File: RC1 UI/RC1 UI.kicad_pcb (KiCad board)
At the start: 2 copper layers, 99.1 x 99.1 mm, 56 parts, among them J1 KB, J2 RC1_UI_Port, J3 COM, M1 Mounting, M2 Mounting, M3 Mounting, M4 Mounting, Q1 2N3906, Q2 2N3906, Q3 2N3906, Q4 2N3906, Q5 2N3906, Q6 2N3906, U1 74LS145, U2 74LS06, U3 74LS38, U4 74LS00

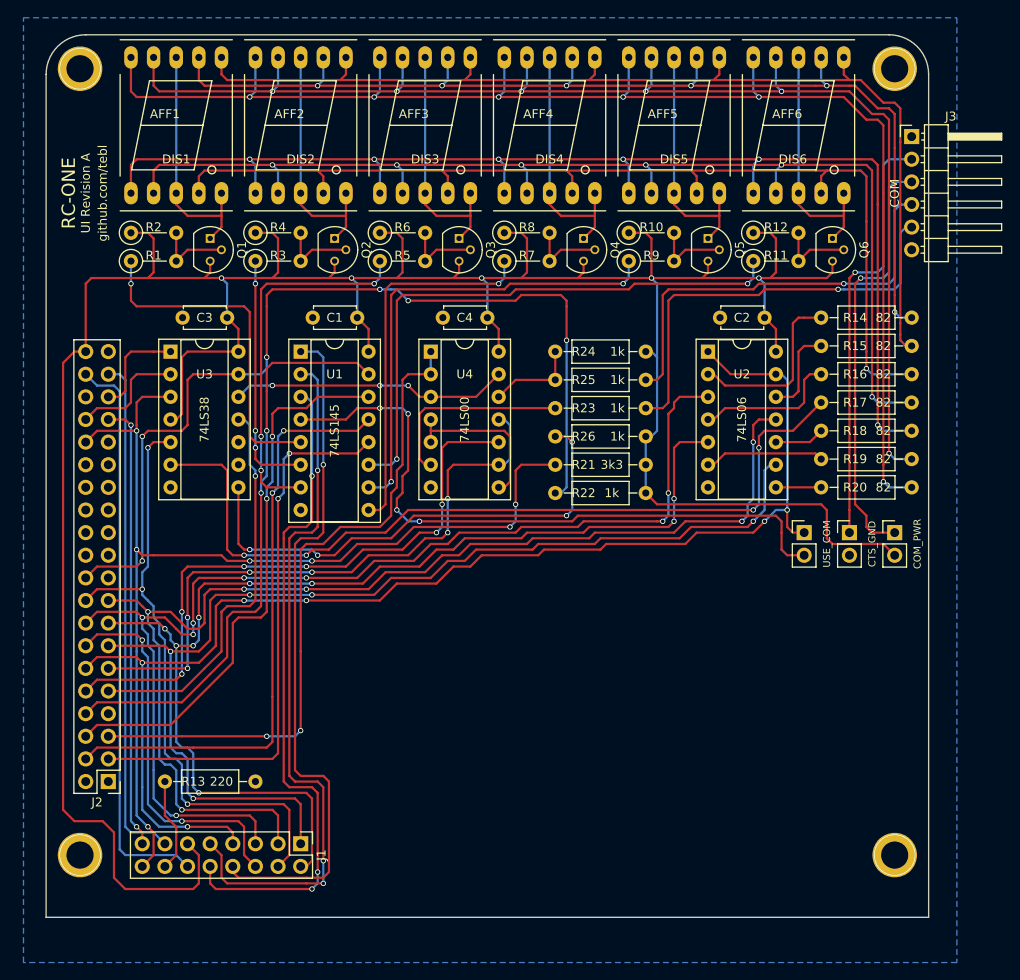
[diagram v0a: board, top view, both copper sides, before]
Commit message: Tweaked silkscreens and exported gerbers for CPU/UI
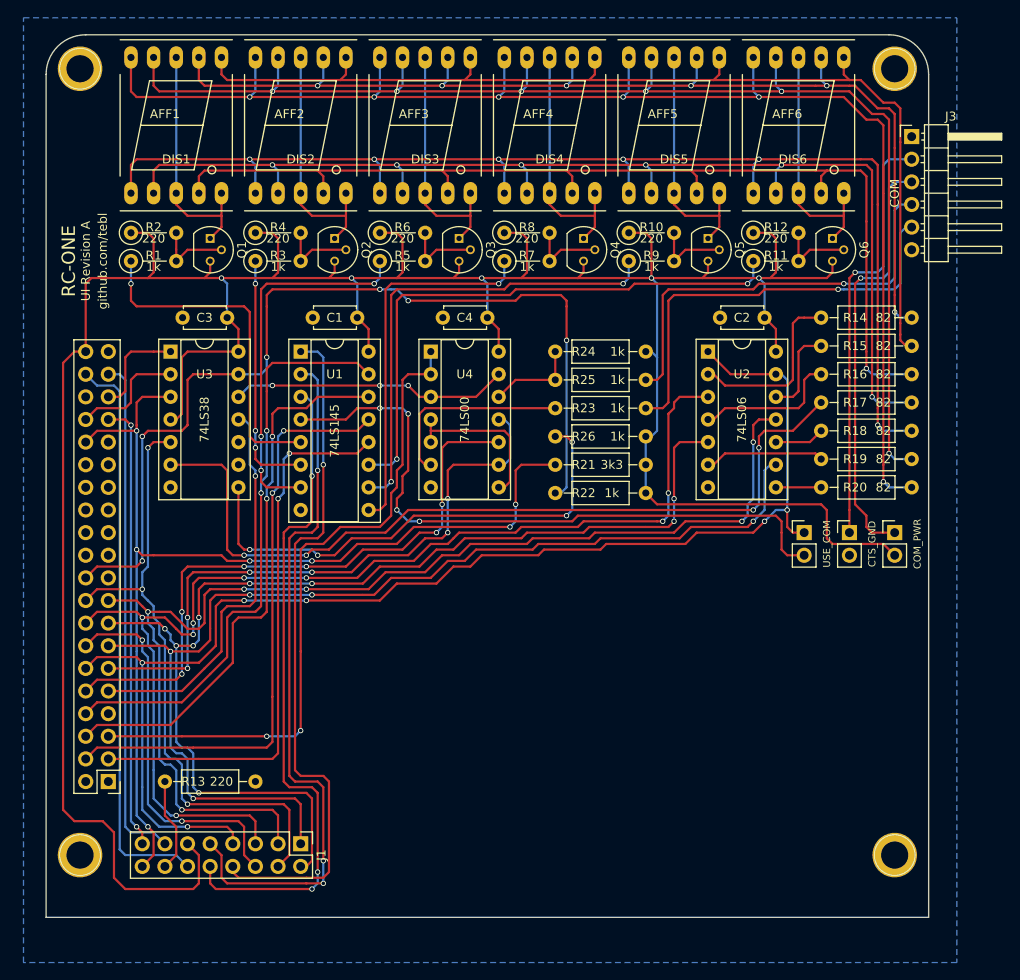
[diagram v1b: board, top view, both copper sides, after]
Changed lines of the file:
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@@
     (descr "Through hole straight pin header, 2x20, 2.54mm pitch, double rows")
     (tags "Through hole pin header THT 2x20 2.54mm double row")
-    (fp_text reference J2 (at 1.27 -2.33 180) (layer F.SilkS)
-      (effects (font (size 1 1) (thickness 0.15)))
-    )
-    (fp_text value RC1_UI_Port (at 1.27 50.59 180) (layer F.Fab)
+    (fp_text reference J2 (at 1.27 -2.54 180) (layer F.Fab)
+      (effects (font (size 1 1) (thickness 0.15)))
+    )
+    (fp_text value RC1_UI_Port (at 1.27 50.8 180) (layer F.Fab)
       (effects (font (size 1 1) (thickness 0.15)))
     )
@@
       (effects (font (size 1 1) (thickness 0.15)))
     )
-    (fp_text value 1k (at 2.54 0.635) (layer F.Fab)
+    (fp_text value 1k (at 2.54 0.635) (layer F.SilkS)
       (effects (font (size 1 1) (thickness 0.15)))
     )
@@
       (effects (font (size 1 1) (thickness 0.15)))
     )
-    (fp_text value 220 (at 2.54 0.635) (layer F.Fab)
+    (fp_text value 220 (at 2.54 0.635) (layer F.SilkS)
       (effects (font (size 1 1) (thickness 0.15)))
     )
@@
       (effects (font (size 1 1) (thickness 0.15)))
     )
-    (fp_text value 1k (at 2.54 0.635) (layer F.Fab)
+    (fp_text value 1k (at 2.54 0.635) (layer F.SilkS)
       (effects (font (size 1 1) (thickness 0.15)))
     )
@@
       (effects (font (size 1 1) (thickness 0.15)))
     )
-    (fp_text value 220 (at 2.54 0.635) (layer F.Fab)
+    (fp_text value 220 (at 2.54 0.635) (layer F.SilkS)
       (effects (font (size 1 1) (thickness 0.15)))
     )
@@
       (effects (font (size 1 1) (thickness 0.15)))
     )
-    (fp_text value 1k (at 2.54 0.635) (layer F.Fab)
+    (fp_text value 1k (at 2.54 0.635) (layer F.SilkS)
       (effects (font (size 1 1) (thickness 0.15)))
     )
@@
       (effects (font (size 1 1) (thickness 0.15)))
     )
-    (fp_text value 220 (at 2.54 0.635) (layer F.Fab)
+    (fp_text value 220 (at 2.54 0.635) (layer F.SilkS)
       (effects (font (size 1 1) (thickness 0.15)))
     )
@@
       (effects (font (size 1 1) (thickness 0.15)))
     )
-    (fp_text value 1k (at 2.54 0.635) (layer F.Fab)
+    (fp_text value 1k (at 2.54 0.635) (layer F.SilkS)
       (effects (font (size 1 1) (thickness 0.15)))
     )
@@
       (effects (font (size 1 1) (thickness 0.15)))
     )
-    (fp_text value 220 (at 2.54 0.635) (layer F.Fab)
+    (fp_text value 220 (at 2.54 0.635) (layer F.SilkS)
       (effects (font (size 1 1) (thickness 0.15)))
     )
@@
       (effects (font (size 1 1) (thickness 0.15)))
     )
-    (fp_text value 1k (at 2.54 0.635) (layer F.Fab)
+    (fp_text value 1k (at 2.54 0.635) (layer F.SilkS)
       (effects (font (size 1 1) (thickness 0.15)))
     )
@@
       (effects (font (size 1 1) (thickness 0.15)))
     )
-    (fp_text value 220 (at 2.54 0.635) (layer F.Fab)
+    (fp_text value 220 (at 2.54 0.635) (layer F.SilkS)
       (effects (font (size 1 1) (thickness 0.15)))
     )
@@
       (effects (font (size 1 1) (thickness 0.15)))
     )
-    (fp_text value 1k (at 2.54 0.635) (layer F.Fab)
+    (fp_text value 1k (at 2.54 0.635) (layer F.SilkS)
       (effects (font (size 1 1) (thickness 0.15)))
     )
@@
       (effects (font (size 1 1) (thickness 0.15)))
     )
-    (fp_text value 220 (at 2.54 0.635) (layer F.Fab)
+    (fp_text value 220 (at 2.54 0.635) (layer F.SilkS)
       (effects (font (size 1 1) (thickness 0.15)))
     )
@@
     )
   )
-  (gr_text "UI Revision A" (at 112.395 54.61 90) (layer F.SilkS)
+  (gr_text "UI Revision A" (at 112.395 62.23 90) (layer F.SilkS)
     (effects (font (size 1 1) (thickness 0.15)))
   )
-  (gr_text github.com/tebl (at 114.3 54.61 90) (layer F.SilkS)
+  (gr_text github.com/tebl (at 114.3 62.23 90) (layer F.SilkS)
     (effects (font (size 1 1) (thickness 0.15)))
   )
-  (gr_text RC-ONE (at 110.49 54.61 90) (layer F.SilkS)
+  (gr_text RC-ONE (at 110.49 62.23 90) (layer F.SilkS)
     (effects (font (size 1.5 1.5) (thickness 0.3)))
   )

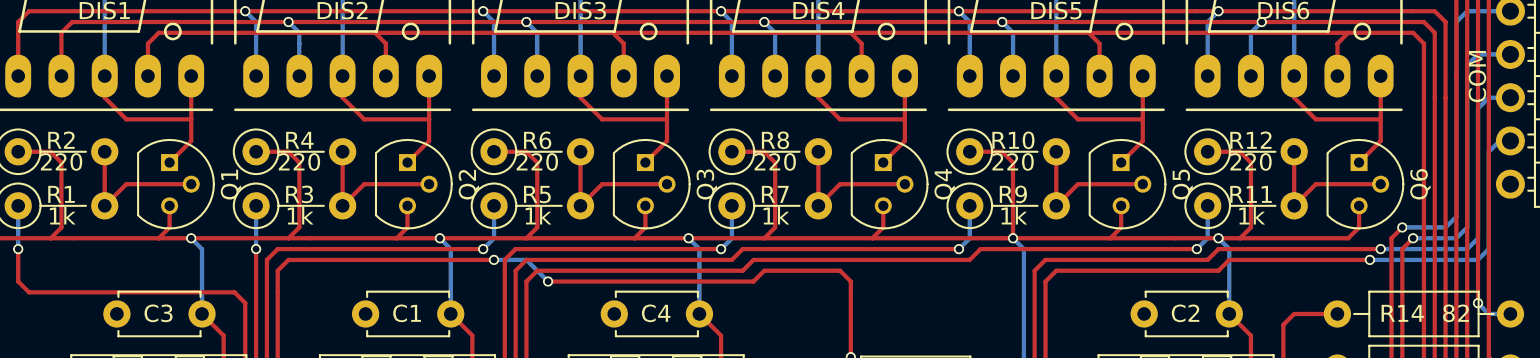
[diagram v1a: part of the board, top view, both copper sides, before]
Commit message: Moved transistors the right way around
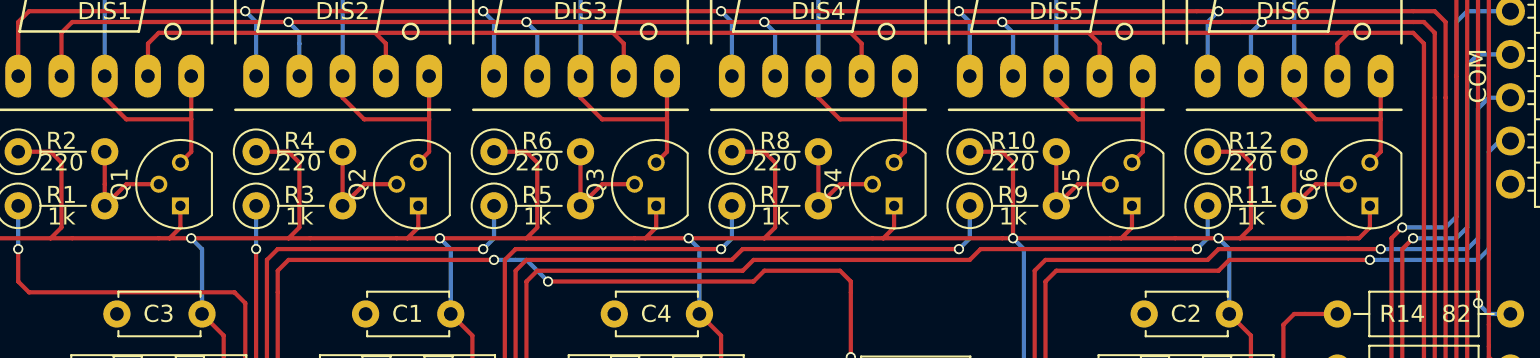
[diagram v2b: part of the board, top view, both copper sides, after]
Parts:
- moved Q1 2.62 mm to (127.0, 62.2), turned to 90 degrees
- moved Q2 2.62 mm to (141.0, 62.2), turned to 90 degrees
- moved Q3 2.62 mm to (154.9, 62.2), turned to 90 degrees
- moved Q4 2.62 mm to (168.9, 62.2), turned to 90 degrees
- moved Q5 2.62 mm to (182.9, 62.2), turned to 90 degrees
- moved Q6 2.62 mm to (196.8, 62.2), turned to 90 degrees
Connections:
- Q1 pad 1: Net-(AFF1-Pad3) -> VCC
- Q1 pad 3: VCC -> Net-(AFF1-Pad3)
- Q2 pad 1: Net-(AFF2-Pad3) -> VCC
- Q2 pad 3: VCC -> Net-(AFF2-Pad3)
- Q3 pad 1: Net-(AFF3-Pad3) -> VCC
- Q3 pad 3: VCC -> Net-(AFF3-Pad3)
- Q4 pad 1: Net-(AFF4-Pad3) -> VCC
- Q4 pad 3: VCC -> Net-(AFF4-Pad3)
- Q5 pad 1: Net-(AFF5-Pad3) -> VCC
- Q5 pad 3: VCC -> Net-(AFF5-Pad3)
- Q6 pad 1: Net-(AFF6-Pad3) -> VCC
- Q6 pad 3: VCC -> Net-(AFF6-Pad3)
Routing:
- net Net-(Q3-Pad2): track 8.78 -> 6.88 mm
- net Net-(Q2-Pad2): track 8.78 -> 6.88 mm
- net Net-(Q6-Pad2): track 8.78 -> 6.88 mm
- net Net-(Q4-Pad2): track 8.78 -> 6.88 mm
- net Net-(Q1-Pad2): track 8.78 -> 6.88 mm
- net Net-(Q5-Pad2): track 8.78 -> 6.88 mm
- net VCC: track 339.4 -> 340.1 mm
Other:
- board text added: "6x 2N3906"

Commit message: Layout updated
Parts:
- removed R10, R12: 220, Resistors_THT:R_Axial_DIN0207_L6.3mm_D2.5mm_P5.08mm_Vertical
- removed R11, R9: 1k, Resistors_THT:R_Axial_DIN0207_L6.3mm_D2.5mm_P5.08mm_Vertical
- removed R24: 1k, Resistors_THT:R_Axial_DIN0207_L6.3mm_D2.5mm_P10.16mm_Horizontal
- added C5: 100nF, Capacitors_THT:C_Disc_D4.7mm_W2.5mm_P5.00mm, F.Cu at (128.3, 68.6)
- added C6: 100nF, Capacitors_THT:C_Disc_D4.7mm_W2.5mm_P5.00mm, F.Cu at (189.2, 68.6)
- added J4: TAPE, Pin_Headers:Pin_Header_Straight_1x04_Pitch2.54mm, F.Cu at (156.2, 130.2)
- added JP4: DP_EN, Pin_Headers:Pin_Header_Straight_1x03_Pitch2.54mm, F.Cu at (200.0, 104.8)
- added JP5: SSD_EN, Pin_Headers:Pin_Header_Straight_1x03_Pitch2.54mm, F.Cu at (195.6, 104.8)
- added JP6: DP4_EN, Pin_Headers:Pin_Header_Straight_1x03_Pitch2.54mm, F.Cu at (204.5, 104.8)
- added U5: 74LS04, Housings_DIP:DIP-14_W7.62mm_Socket, F.Cu at (121.9, 72.4)
- added U6: 74LS244, Housings_DIP:DIP-20_W7.62mm_Socket, F.Cu at (182.9, 72.4)
- J1: value KB -> KEYPAD
- J3: moved to B.Cu
- JP2: value CTS_GND -> FlowControl; footprint Pin_Headers:Pin_Header_Straight_1x02_Pitch2.54mm -> Pin_Headers:Pin_Header_Angled_1x02_Pitch2.54mm; moved to B.Cu
- Q1, Q2, Q3, Q4, Q5, Q6: value 2N3906 -> 2N3904
- R1, R3, R5: value 1k -> 10k
- R14, R15, R16, R17, R18, R19, R20: value 82 -> 100
- R2, R4, R6: value 220 -> 10k
- R21: value 3k3 -> 10k
- R7: value 1k -> 100; footprint Resistors_THT:R_Axial_DIN0207_L6.3mm_D2.5mm_P5.08mm_Vertical -> Resistors_THT:R_Axial_DIN0207_L6.3mm_D2.5mm_P10.16mm_Horizontal
- R8: value 220 -> 100; footprint Resistors_THT:R_Axial_DIN0207_L6.3mm_D2.5mm_P5.08mm_Vertical -> Resistors_THT:R_Axial_DIN0207_L6.3mm_D2.5mm_P10.16mm_Horizontal
- U1: value 74LS145 -> 74LS138
- U2: value 74LS06 -> 74LS138; footprint Housings_DIP:DIP-14_W7.62mm_Socket -> Housings_DIP:DIP-16_W7.62mm_Socket
- U3: value 74LS38 -> 74LS01
- moved R8 54.5 mm to (194.9, 100.3)
- moved R22 47.6 mm to (134.6, 113.0), turned to 0 degrees
- moved R6 46.4 mm to (191.8, 59.1), turned to 180 degrees
- moved R26 46.4 mm to (144.8, 116.8)
- moved R21 38.9 mm to (134.6, 109.2)
- moved R7 37.8 mm to (194.9, 74.9)
- moved JP1 35.4 mm to (197.5, 127.6)
- moved C3 33.0 mm to (128.3, 101.6)
- moved U3 33.0 mm to (121.9, 105.4)
- moved R5 32.5 mm to (177.8, 59.1), turned to 180 degrees
- moved R4 32.4 mm to (163.8, 59.1), turned to 180 degrees
- moved C2 29.8 mm to (158.8, 68.6)
- moved U2 29.8 mm to (152.4, 72.4)
- moved JP2 28.8 mm to (205.1, 64.8)
- moved JP3 22.6 mm to (179.1, 74.9)
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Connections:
- AFF1 pad 5: Net-(AFF1-Pad3) -> /DP
- AFF2 pad 5: Net-(AFF2-Pad3) -> /DP
- AFF3 pad 5: Net-(AFF3-Pad3) -> /DP
- AFF4 pad 5: Net-(AFF4-Pad3) -> /DP4
- AFF5 pad 5: Net-(AFF5-Pad3) -> /DP
- AFF6 pad 5: Net-(AFF6-Pad3) -> /DP
- J1 pad 14: /KP_PWR -> Net-(J1-Pad14)
- J1 pad 15: SST_OUT -> SST_IN
- J1 pad 16: SST_IN -> SST_OUT
- J2 pad 20: TAPE -> (no net)
- J2 pad 32: SST_IN -> (no net)
- J2 pad 7: (no net) -> /PB6
- J3 pad 1: GND -> Net-(J3-Pad1)
- J3 pad 6: (no net) -> GND
- JP1 pad 1: Net-(J3-Pad3) -> Net-(J3-Pad4)
- JP2 pad 1: Net-(J3-Pad2) -> Net-(J3-Pad1)
- JP2 pad 2: GND -> Net-(J3-Pad5)
- JP3 pad 2: Net-(JP3-Pad2) -> /MODE
- Q1 pad 1: VCC -> GND
- Q2 pad 1: VCC -> GND
- Q3 pad 1: VCC -> GND
- Q4 pad 1: VCC -> GND
- Q5 pad 1: VCC -> GND
- Q6 pad 1: VCC -> GND
- R1 pad 1: Net-(R1-Pad1) -> Net-(Q1-Pad2)
- R1 pad 2: Net-(Q1-Pad2) -> /DIS1
- R13 pad 1: GND -> Net-(J1-Pad14)
- R13 pad 2: /KP_PWR -> GND
- R2 pad 1: VCC -> Net-(Q2-Pad2)
- R2 pad 2: Net-(Q1-Pad2) -> /DIS2
- R22 pad 1: VCC -> Net-(J4-Pad2)
- R22 pad 2: TAPE -> VCC
- R23 pad 1: Net-(J3-Pad5) -> /TX
- R23 pad 2: /TX -> Net-(J3-Pad2)
- R25 pad 1: Net-(J3-Pad4) -> /RX
- R25 pad 2: /RX -> Net-(J3-Pad3)
- R3 pad 1: Net-(R3-Pad1) -> Net-(Q3-Pad2)
- R3 pad 2: Net-(Q2-Pad2) -> /DIS3
- R4 pad 1: VCC -> Net-(Q4-Pad2)
- R4 pad 2: Net-(Q2-Pad2) -> /DIS4
- R5 pad 1: Net-(R5-Pad1) -> Net-(Q5-Pad2)
- R5 pad 2: Net-(Q3-Pad2) -> /DIS5
- R6 pad 1: VCC -> Net-(Q6-Pad2)
- R6 pad 2: Net-(Q3-Pad2) -> /DIS6
- R7 pad 2: Net-(Q4-Pad2) -> /DP
- R8 pad 2: Net-(Q4-Pad2) -> Net-(JP6-Pad1)
- U1 pad 1: /ROW0 -> /PB1
- U1 pad 12: /PB4 -> /MODE
- U1 pad 13: /PB3 -> /ROW2
- U1 pad 14: /PB2 -> /ROW1
- U1 pad 15: /PB1 -> /ROW0
- U1 pad 2: /ROW1 -> /PB2
- U1 pad 3: /ROW2 -> /PB3
- U1 pad 4: Net-(JP3-Pad2) -> GND
- U1 pad 5: Net-(R1-Pad1) -> /PB4
- U1 pad 6: Net-(R3-Pad1) -> VCC
- U1 pad 7: Net-(R5-Pad1) -> Net-(U1-Pad7)
- U1 pad 9: Net-(R7-Pad1) -> Net-(U1-Pad9)
- U2 pad 1: /PA0 -> /PB1
- U2 pad 10: Net-(R18-Pad1) -> (no net)
- U2 pad 11: /PA4 -> (no net)
- U2 pad 12: Net-(R15-Pad1) -> (no net)
- U2 pad 13: /PA0 -> (no net)
- U2 pad 14: VCC -> Net-(U2-Pad14)
- U2 pad 2: Net-(R14-Pad1) -> /PB2
- U2 pad 3: /PA2 -> /PB3
- U2 pad 4: Net-(R16-Pad1) -> GND
- U2 pad 5: /PA5 -> GND
- U2 pad 6: Net-(R19-Pad1) -> /PB4
- U2 pad 7: GND -> (no net)
- U2 pad 8: Net-(R20-Pad1) -> GND
- U2 pad 9: /PA6 -> (no net)
- U3 pad 1: K7 -> SST_IN
- U3 pad 10: GND -> Net-(R26-Pad2)
- U3 pad 11: /PB7 -> VCC
- U3 pad 12: Net-(U3-Pad12) -> /PB7
- U3 pad 13: TAPE -> Net-(J4-Pad2)
- U3 pad 2: SYNC -> K7
- U3 pad 3: SST_IN -> SYNC
- U3 pad 4: VCC -> Net-(R26-Pad2)
- U3 pad 5: /PA3 -> GND
- U3 pad 6: Net-(R17-Pad1) -> GND
- U3 pad 8: Net-(R26-Pad2) -> GND
- U4 pad 11: /PA7 -> /PB7
- U4 pad 12: /RX -> Net-(U4-Pad12)
- U4 pad 13: Net-(U3-Pad12) -> Net-(J4-Pad3)
- U4 pad 3: Net-(U3-Pad12) -> Net-(U4-Pad12)
- U4 pad 4: Net-(U4-Pad4) -> Net-(U4-Pad12)
- U4 pad 5: Net-(U4-Pad4) -> /RX
- U4 pad 6: /TX -> /PA7
- U4 pad 8: Net-(U4-Pad4) -> /TX
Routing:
- net /DP: track 0.00 -> 154.3 mm, vias 0 -> 3
- net /PB6: track 0.00 -> 114.4 mm, vias 0 -> 1
- net TAPE: track 106.9 -> 0.00 mm, vias 6 -> 0
- net /PA1: track 42.6 -> 133.4 mm, vias 2 -> 4
- net /DP4: track 0.00 -> 89.6 mm
- net Net-(R17-Pad1): track 94.0 -> 7.40 mm, vias 4 -> 0
- net SST_IN: track 119.7 -> 38.5 mm, vias 7 -> 1
- net /DIS6: track 0.00 -> 78.0 mm, vias 0 -> 1
- net Net-(J4-Pad3): track 0.00 -> 74.9 mm, vias 0 -> 2
- net Net-(JP3-Pad2): track 74.4 -> 0.00 mm, vias 4 -> 0
- net VCC: track 340.1 -> 411.6 mm, vias 5 -> 8
- net /DIS5: track 0.00 -> 70.8 mm, vias 0 -> 1
- net /DIS4: track 0.00 -> 63.5 mm, vias 0 -> 1
- net /PB7: track 44.8 -> 101.1 mm, vias 1 -> 4
- net /MODE: track 0.00 -> 53.6 mm, vias 0 -> 1
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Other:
- board size 99.1 x 99.1 mm -> 99.1 x 97.2 mm
- board text added: "$00F9"
- board text added: "$00FA"
- board text added: "$00FB"
- board text added: "$17FA $17FB $17FE $17FF"
- board text added: "(C.K.)"
- board text added: "00 1C 00 1C"
- board text added: "1"
- board text added: "6x 2N3904"
- board text added: "7 SEGMENT DISPLAYS"
- board text added: "7SEGMENT ENABLE"
- board text added: "COM"
- board text added: "CONNECT PB6 TO DP"
- board text added: "DEVICE SELECT"
- board text added: "DISPLAY BUFFER"
- board text added: "DP EN."
- board text added: "DP4 ALWAYS ON"
- board text added: "DP4 ON"
- board text added: "GND"
- board text added: "HEX INVERTER"
- board text added: "NAND GATES"
- board text added: "NAND GATES (OC)"
- board text added: "POWER RC-ONE OVER USB (NO EXTERNAL POWER)"
- board text added: "RC-ONE KEYPAD"
- board text added: "RXD"
- board text added: "SSD EN."
- board text added: "TAPE (5V)"
- board text added: "TAPE (TTL LEVEL)"
- board text added: "TTY MODE"
- board text added: "TXD"
- board text added: "UI Revision B"
- board text added: "~CTS-RTS"
- board text removed: "6x 2N3906"
- board text removed: "UI Revision A"
